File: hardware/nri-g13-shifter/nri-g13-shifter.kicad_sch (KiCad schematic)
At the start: 39 parts, among them J1 NRI G-13 (10 pin), J2 RP2350-Plus, J3 +12V IN, Q1 BSS138, Q2 BSS138, Q3 BSS138, Q4 BSS138, Q5 BSS138, Q6 BSS138, Q7 BSS138

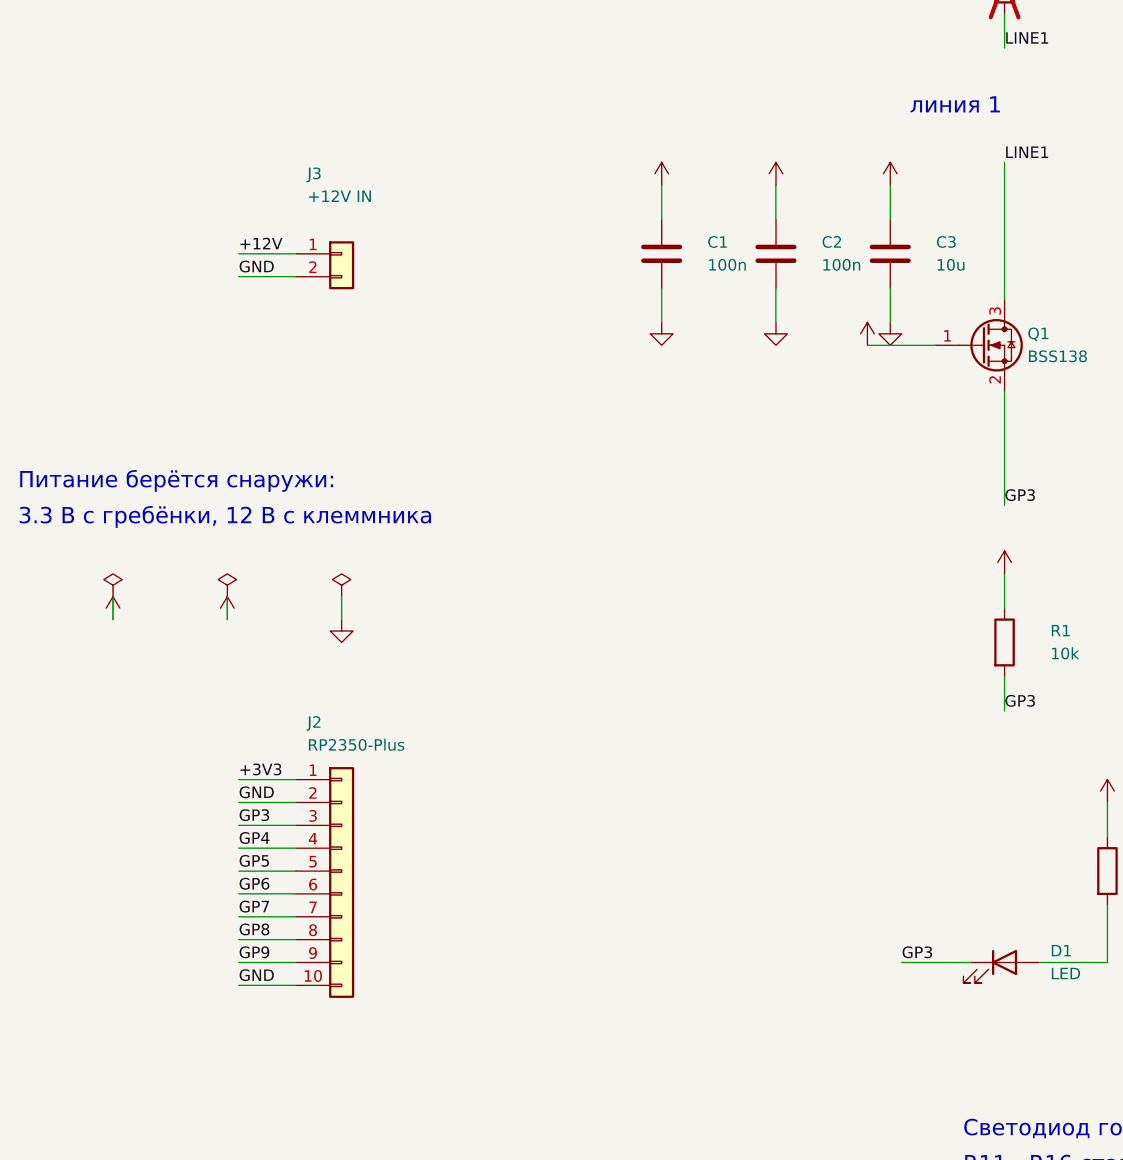
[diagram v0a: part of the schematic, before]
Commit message: Плата компактнее на треть, 12 В переехало в гребёнку
Клеммник убран, питание приёмника идёт через ту же гребёнку, что и
сигналы: отдельный разъём означал бы второй кабель к устройству, которое
и так стоит в тесном корпусе. Гребёнка стала двенадцатиконтактной, а
сигнальные выводы по-прежнему идут подряд и в порядке строк платы —
от этого веер разводки остаётся непересекающимся сам собой.

Плата 78x79 мм вместо 96x92, площадь меньше на 30%. Строка канала сжата
с 10 до 8 мм: полосы внутри неё не перекрываются по горизонтали, поэтому
индикатор и отвод к разъёму удалось посадить на одну высоту. По ширине
убраны просветы между шинами питания.

Попутно вылезла закономерность, которую пришлось записать в код: из двух
цепей, уходящих наверх по соседним вертикалям, выше должна идти та, что
взяла внешнюю вертикаль. Иначе её горизонталь пересекает чужую. DRC
поймал это дважды, пока порядок не встал правильно.

Проверено: ERC 0, DRC 0, неразведённых 0, расхождений со схемой 0.

Co-Authored-By: Claude Opus 5 (1M context) <noreply@anthropic.com>
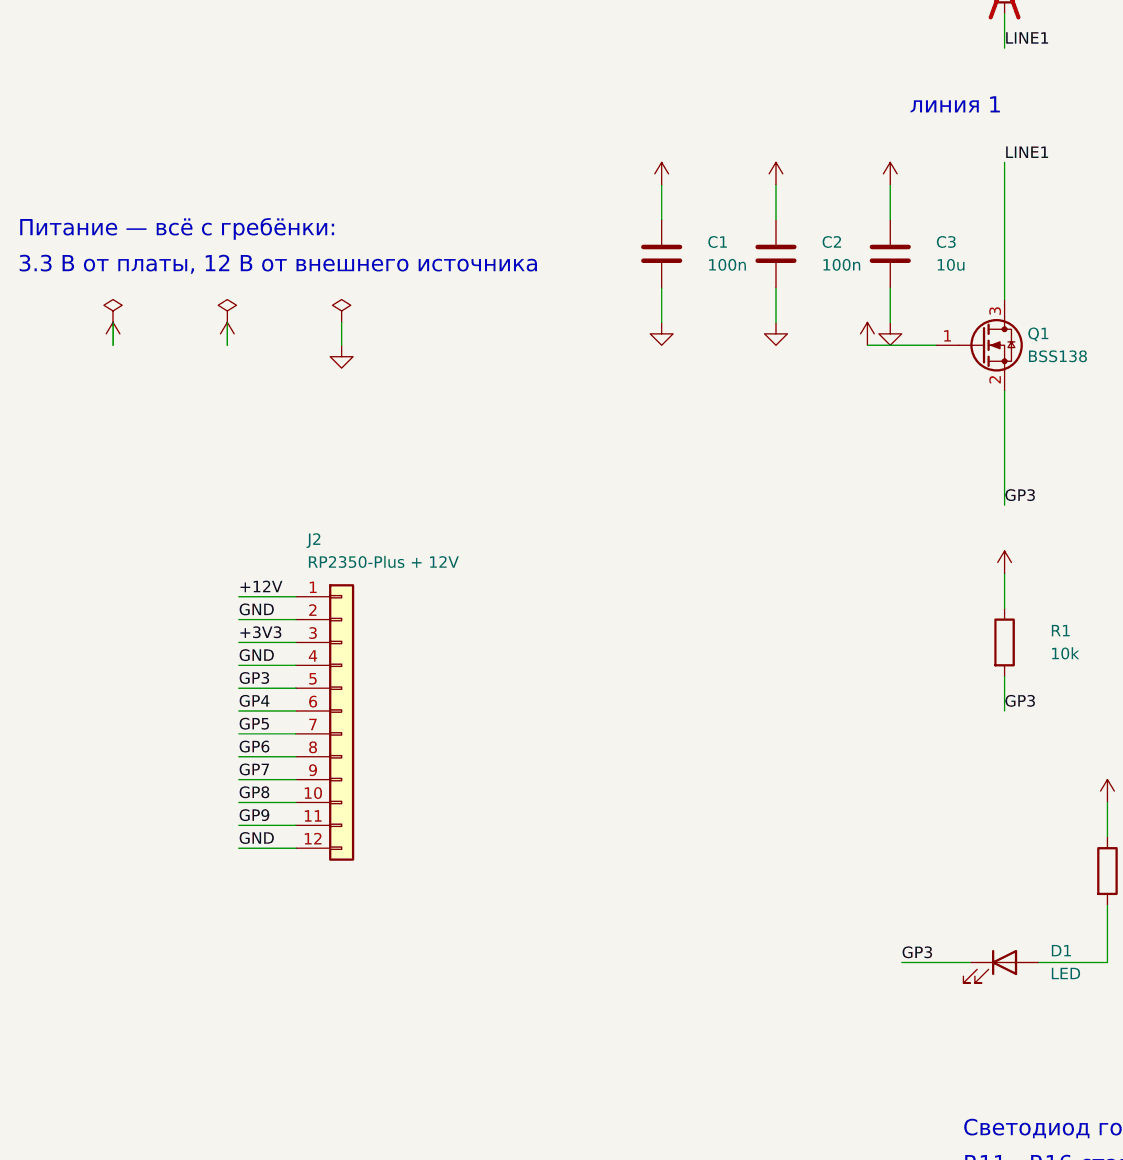
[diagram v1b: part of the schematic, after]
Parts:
- removed J2: RP2350-Plus, Connector_PinHeader_2.54mm:PinHeader_1x10_P2.54mm_Vertical, symbol Connector_Generic:Conn_01x10
- removed J3: +12V IN, TerminalBlock_Phoenix:TerminalBlock_Phoenix_MKDS-1,5-2-5.08_1x02_P5.08mm_Horizontal, symbol Connector_Generic:Conn_01x02
- added J2: RP2350-Plus + 12V, Connector_PinHeader_2.54mm:PinHeader_1x12_P2.54mm_Vertical, symbol Connector_Generic:Conn_01x12
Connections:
- net +12V: now also J2.1 (Pin_1)
- net +3V3: now also J2.3 (Pin_3)
- net GND: now also J2.12 (Pin_12), J2.2 (Pin_2), J2.4 (Pin_4)
- net GP3: now also J2.5 (Pin_5)
- net GP4: now also J2.6 (Pin_6)
- net GP5: now also J2.7 (Pin_7)
- net GP6: now also J2.8 (Pin_8)
- net GP7: now also J2.9 (Pin_9)
- net GP8: now also J2.10 (Pin_10)
- net GP9: now also J2.11 (Pin_11)
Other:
- note added: "3.3 В от платы, 12 В от внешнего источника"
- note added: "Питание — всё с гребёнки:"
- note removed: "3.3 В с гребёнки, 12 В с клеммника"
- note removed: "Питание берётся снаружи:"

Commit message: Артикулы JLCPCB и исправление номинала C3
Артикулы проставлены в схеме, при компонентах, и оттуда попадают и в
bom.csv, и в плату. Все сверены по каталогу, а не восстановлены по
памяти: неверный код — это не опечатка, а другая деталь на плате.

Подбор артикулов и вскрыл ошибку: C3 стоял на 10 мкФ, а в корпусе 0603
такая ёмкость бывает только на 10 вольт. Сидит эта банка на шине 12 В,
то есть номинал был просто неработоспособен. В схеме этого не видно —
там написано «10u» без напряжения, — а в каталоге написано. Поставлено
1 мкФ 50 В, тока тут копеечный и ёмкости хватает с запасом.

BSS138 оставлен расширенной позицией. Базовый 2N7002 сэкономил бы плату
за настройку станка, но у него порог отпирания вдвое выше, а весь смысл
каскада в том, чтобы он открывался от 3.3 В.

Артикул переносится и в посадочные места платы: иначе сверка со схемой
считает поле потерянным, а на монтаж уедет плата без указания, что
ставить.

Проверено: ERC 0, DRC 0, расхождений со схемой 0.

Co-Authored-By: Claude Opus 5 (1M context) <noreply@anthropic.com>
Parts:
- C1, C2: LCSC (none) -> C14663
- C3: value 10u -> 1u; LCSC (none) -> C15849
- D1, D2, D3, D4, D5, D6: LCSC (none) -> C72043
- Q1, Q2, Q3, Q4, Q5, Q6, Q7: LCSC (none) -> C78284
- R1, R11, R12, R13, R14, R15, R16, R17, R2, R3, R4, R5, R6, R7: LCSC (none) -> C25804
- R21, R22, R23, R24, R25, R26: LCSC (none) -> C21190

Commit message: Светодиод красный, резистор 470 Ом: зелёный не зажёгся бы вовсе
JLCPCB не сопоставил C72043 — снят с наличия. При проверке замены
выяснилось худшее: у зелёного в корпусе 0603 прямое напряжение 3.3 В,
ровно столько же, сколько на шине, от которой он питается. Через 1 кОм
ток получался бы нулевой, и шесть индикаторов просто не горели бы.

Красный C2286 (KT-0603R): 1.8…2.4 В, склад под четыре миллиона штук.
Резистор заодно уменьшен до 470 Ом — около 3 мА, для вспышки длиной
100 мс этого хватает уверенно.

Второй раз подряд ошибку вскрывает подбор артикулов, а не схема: в
номиналах «10u» и «LED» нет ни рабочего напряжения, ни прямого падения,
а в каталоге есть.

Проверено: ERC 0, DRC 0, расхождений со схемой 0.

Co-Authored-By: Claude Opus 5 (1M context) <noreply@anthropic.com>
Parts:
- D1, D2, D3, D4, D5, D6: LCSC C72043 -> C2286
- R21, R22, R23, R24, R25, R26: value 1k -> 470; LCSC C21190 -> C23179
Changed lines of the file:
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@@
 			(effects (font (size 1.27 1.27)) (hide yes))
 		)
-		(property "LCSC" "C72043"
+		(property "LCSC" "C2286"
 			(at 134.62 180.34 0)
 			(effects (font (size 1.27 1.27)) (hide yes))
@@
 			(effects (font (size 1.27 1.27)) (justify left))
 		)
-		(property "Value" "1k"
+		(property "Value" "470"
 			(at 151.13000000000002 171.45 0)
 			(effects (font (size 1.27 1.27)) (justify left))
@@
 			(effects (font (size 1.27 1.27)) (hide yes))
 		)
-		(property "LCSC" "C21190"
+		(property "LCSC" "C23179"
 			(at 146.05 170.18 0)
 			(effects (font (size 1.27 1.27)) (hide yes))
@@
 			(effects (font (size 1.27 1.27)) (hide yes))
 		)
-		(property "LCSC" "C72043"
+		(property "LCSC" "C2286"
 			(at 167.64 180.34 0)
 			(effects (font (size 1.27 1.27)) (hide yes))
@@
 			(effects (font (size 1.27 1.27)) (justify left))
 		)
-		(property "Value" "1k"
+		(property "Value" "470"
 			(at 184.15 171.45 0)
 			(effects (font (size 1.27 1.27)) (justify left))
@@
 			(effects (font (size 1.27 1.27)) (hide yes))
 		)
-		(property "LCSC" "C21190"
+		(property "LCSC" "C23179"
 			(at 179.07 170.18 0)
 			(effects (font (size 1.27 1.27)) (hide yes))
@@
 			(effects (font (size 1.27 1.27)) (hide yes))
 		)
-		(property "LCSC" "C72043"
+		(property "LCSC" "C2286"
 			(at 200.66 180.34 0)
 			(effects (font (size 1.27 1.27)) (hide yes))
@@
 			(effects (font (size 1.27 1.27)) (justify left))
 		)
-		(property "Value" "1k"
+		(property "Value" "470"
 			(at 217.17000000000002 171.45 0)
 			(effects (font (size 1.27 1.27)) (justify left))
@@
 			(effects (font (size 1.27 1.27)) (hide yes))
 		)
-		(property "LCSC" "C21190"
+		(property "LCSC" "C23179"
 			(at 212.09 170.18 0)
 			(effects (font (size 1.27 1.27)) (hide yes))
@@
 			(effects (font (size 1.27 1.27)) (hide yes))
 		)
-		(property "LCSC" "C72043"
+		(property "LCSC" "C2286"
 			(at 233.68 180.34 0)
 			(effects (font (size 1.27 1.27)) (hide yes))
@@
 			(effects (font (size 1.27 1.27)) (justify left))
 		)
-		(property "Value" "1k"
+		(property "Value" "470"
 			(at 250.19000000000003 171.45 0)
 			(effects (font (size 1.27 1.27)) (justify left))
@@
 			(effects (font (size 1.27 1.27)) (hide yes))
 		)
-		(property "LCSC" "C21190"
+		(property "LCSC" "C23179"
 			(at 245.11 170.18 0)
 			(effects (font (size 1.27 1.27)) (hide yes))
@@
 			(effects (font (size 1.27 1.27)) (hide yes))
 		)
-		(property "LCSC" "C72043"
+		(property "LCSC" "C2286"
 			(at 266.70000000000005 180.34 0)
 			(effects (font (size 1.27 1.27)) (hide yes))
@@
 			(effects (font (size 1.27 1.27)) (justify left))
 		)
-		(property "Value" "1k"
+		(property "Value" "470"
 			(at 283.21000000000004 171.45 0)
 			(effects (font (size 1.27 1.27)) (justify left))
@@
 			(effects (font (size 1.27 1.27)) (hide yes))
 		)
-		(property "LCSC" "C21190"
+		(property "LCSC" "C23179"
 			(at 278.13000000000005 170.18 0)
 			(effects (font (size 1.27 1.27)) (hide yes))
@@
 			(effects (font (size 1.27 1.27)) (hide yes))
 		)
-		(property "LCSC" "C72043"
+		(property "LCSC" "C2286"
 			(at 299.72 180.34 0)
 			(effects (font (size 1.27 1.27)) (hide yes))
@@
 			(effects (font (size 1.27 1.27)) (justify left))
 		)
-		(property "Value" "1k"
+		(property "Value" "470"
 			(at 316.23 171.45 0)
 			(effects (font (size 1.27 1.27)) (justify left))
@@
 			(effects (font (size 1.27 1.27)) (hide yes))
 		)
-		(property "LCSC" "C21190"
+		(property "LCSC" "C23179"
 			(at 311.15000000000003 170.18 0)
 			(effects (font (size 1.27 1.27)) (hide yes))
